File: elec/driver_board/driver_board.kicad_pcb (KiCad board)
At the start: 2 copper layers, 263.5 x 52 mm, 110 parts, among them IC1 TPIC6C595DG4, IC10 TPIC6C595DG4, IC11 TPIC6C595DG4, IC12 TPIC6C595DG4, IC13 TPIC6C595DG4, IC14 TPIC6C595DG4, IC15 TPIC6C595DG4, IC16 TPIC6C595DG4, IC17 TPIC6C595DG4, IC18 TPIC6C595DG4, IC19 TPIC6C595DG4, IC2 TPIC6C595DG4, IC20 TPIC6C595DG4, IC21 TPIC6C595DG4, IC22 TPIC6C595DG4, IC23 TPIC6C595DG4, IC24 TPIC6C595DG4, IC3 TPIC6C595DG4, IC4 TPIC6C595DG4, IC5 TPIC6C595DG4, IC6 TPIC6C595DG4, IC7 TPIC6C595DG4, IC8 TPIC6C595DG4, IC9 TPIC6C595DG4, J1 Connector to the motor board, J10 Connector to the motor board, J11 Connector to the motor board, J12 Connector to the motor board, J13 Connector to the motor board, J14 Connector to the motor board, J15 Connector to the motor board, J16 Connector to the motor board, J17 Connector to the motor board, J18 Connector to the motor board, J19 Connector to the motor board, J2 Connector to the motor board, J20 Connector to the motor board, J21 Connector to the motor board, J22 Connector to the motor board, J23 Connector to the motor board, J24 Connector to the motor board, J25 button_shutdown, J26 button_mode, J27 rotary_encoder, J28 DCF77 board, J29 RTC, J3 Connector to the motor board, J4 Connector to the motor board, J5 Connector to the motor board, J6 Connector to the motor board, J7 Connector to the motor board, J8 Connector to the motor board, J9 Connector to the motor board, U1 ESP32-C3-DEVKITM-1

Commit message: [elec] First version of the routing of driver board
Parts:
- added Cl2: 4.2nF, Capacitor_SMD:C_1206_3216Metric, F.Cu at (81.5, 151.8)
- added Rl2: 4.7k, Capacitor_SMD:C_1206_3216Metric, F.Cu at (81.5, 149.2)
- moved C31 156.5 mm to (88.6, 129.4), turned to 180 degrees
- moved C32 151.1 mm to (88.6, 125.4), turned to 180 degrees
- moved J19 148.4 mm to (117.5, 108.2), turned to 90 degrees
- moved J6 147.6 mm to (161.3, 157.5), turned to 90 degrees
- moved J7 144.6 mm to (175.9, 157.5), turned to 90 degrees
- moved J17 144.2 mm to (88.2, 108.2), turned to 90 degrees
- moved C37 142.8 mm to (124.8, 93.8), turned to 0 degrees
- moved C38 141.3 mm to (124.8, 97.8), turned to 0 degrees
- moved IC16 141.0 mm to (88.3, 118.0), turned to 180 degrees
- moved C33 140.9 mm to (95.5, 93.8), turned to 0 degrees
- moved J18 140.5 mm to (102.9, 108.2), turned to 90 degrees
- moved IC6 139.3 mm to (168.9, 154.4), turned to 0 degrees
- moved J1 139.2 mm to (88.2, 157.5), turned to 90 degrees
- moved C34 138.8 mm to (95.5, 97.8), turned to 0 degrees
- moved IC19 138.5 mm to (125.1, 105.2), turned to 0 degrees
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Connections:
- net HALL_IN renamed HALL_0_OUTPUT
- J1 pad 10: unconnected-(J1-Pin_10-Pad10) -> HALL_1_OUTPUT
- J10 pad 10: unconnected-(J10-Pin_10-Pad10) -> HALL_1_OUTPUT
- J11 pad 10: unconnected-(J11-Pin_10-Pad10) -> HALL_1_OUTPUT
- J12 pad 10: unconnected-(J12-Pin_10-Pad10) -> HALL_1_OUTPUT
- J13 pad 10: unconnected-(J13-Pin_10-Pad10) -> HALL_1_OUTPUT
- J14 pad 10: unconnected-(J14-Pin_10-Pad10) -> HALL_1_OUTPUT
- J15 pad 10: unconnected-(J15-Pin_10-Pad10) -> HALL_1_OUTPUT
- J16 pad 10: unconnected-(J16-Pin_10-Pad10) -> HALL_1_OUTPUT
- J17 pad 10: unconnected-(J17-Pin_10-Pad10) -> HALL_1_OUTPUT
- J18 pad 10: unconnected-(J18-Pin_10-Pad10) -> HALL_1_OUTPUT
- J19 pad 10: unconnected-(J19-Pin_10-Pad10) -> HALL_1_OUTPUT
- J2 pad 10: unconnected-(J2-Pin_10-Pad10) -> HALL_1_OUTPUT
- J20 pad 10: unconnected-(J20-Pin_10-Pad10) -> HALL_1_OUTPUT
- J21 pad 10: unconnected-(J21-Pin_10-Pad10) -> HALL_1_OUTPUT
- J22 pad 10: unconnected-(J22-Pin_10-Pad10) -> HALL_1_OUTPUT
- J23 pad 10: unconnected-(J23-Pin_10-Pad10) -> HALL_1_OUTPUT
- J24 pad 10: unconnected-(J24-Pin_10-Pad10) -> HALL_1_OUTPUT
- J29 pad 3: /control_board/SDA_TRC -> /control_board/SDA_RTC
- J3 pad 10: unconnected-(J3-Pin_10-Pad10) -> HALL_1_OUTPUT
- J4 pad 10: unconnected-(J4-Pin_10-Pad10) -> HALL_1_OUTPUT
- J5 pad 10: unconnected-(J5-Pin_10-Pad10) -> HALL_1_OUTPUT
- J6 pad 10: unconnected-(J6-Pin_10-Pad10) -> HALL_1_OUTPUT
- J7 pad 10: unconnected-(J7-Pin_10-Pad10) -> HALL_1_OUTPUT
- J8 pad 10: unconnected-(J8-Pin_10-Pad10) -> HALL_1_OUTPUT
- J9 pad 10: unconnected-(J9-Pin_10-Pad10) -> HALL_1_OUTPUT
- U1 pad 21: unconnected-(U1-IO5-Pad21) -> HALL_1_OUTPUT
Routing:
- net HALL_1_OUTPUT: track 0.00 -> 399.0 mm, vias 0 -> 1
- net VCC_3V3: track 0.00 -> 126.5 mm
- net SHIFT_CLOCK: track 572.2 -> 482.1 mm, vias 24 -> 26
- net /control_board/AM_DATA: track 0.00 -> 64.9 mm, vias 0 -> 1
- net VCC: track 720.5 -> 781.4 mm, vias 46 -> 50
- net LATCH_CLOCK: track 500.2 -> 442.1 mm
- net /control_board/PIN_BUTTON_ENCODER: track 0.00 -> 47.6 mm, vias 0 -> 1
- net /control_board/DATA_OUT: track 59.4 -> 18.8 mm
- net /control_board/PIN_ENCODER_1: track 0.00 -> 40.4 mm, vias 0 -> 1
- net /control_board/PIN_ENCODER_0: track 0.00 -> 37.7 mm, vias 0 -> 1
- net /motor_driver10/DATA_IN: track 58.9 -> 22.0 mm, vias 4 -> 0
- net /control_board/SDA_RTC: track 0.00 -> 36.7 mm
- net /control_board/SCL_RTC: track 0.00 -> 34.6 mm
- net /motor_driver8/DATA_OUT: track 55.4 -> 22.2 mm
- net /motor_driver5/DATA_OUT: track 54.8 -> 22.0 mm
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- added copper zone on B.Cu, net GND
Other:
- board size 263.5 x 52 mm -> 170.8 x 83 mm
- board text added: "Driver board V1 26/11/2024"

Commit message: [elec] Add space for physical button
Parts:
- added S1: FSM2JAH, Samacsys:FSM4JH, F.Cu at (42.5, 145.5)
- added S2: FSM2JAH, Samacsys:FSM4JH, F.Cu at (49.0, 145.5)
- Cl1, Cl2: value 4.2nF -> 4.7nF
- moved J25 6.49 mm to (43.5, 156.5)
- moved J26 6.49 mm to (48.0, 156.5)
- moved R1 6.49 mm to (43.5, 152.5)
- moved R2 6.49 mm to (51.0, 155.5)
- moved JP1 5.02 mm to (47.0, 162.8)
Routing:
- net VCC_3V3: track 126.5 -> 151.4 mm
- net /control_board/PIN_BUTTON_MODE: track 6.46 -> 15.9 mm
- net VCC: track 781.4 -> 786.2 mm
- net /control_board/PIN_BUTTON_SHUTDOWN: track 15.0 -> 18.0 mm
- added copper zone on F.Cu, net VCC
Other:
- board size 170.8 x 83 mm -> 171.8 x 83 mm
- board text added: "Driver board v1 26/11/2024"
- board text added: "VCC_3V3"
- board text removed: "Driver board V1 26/11/2024"

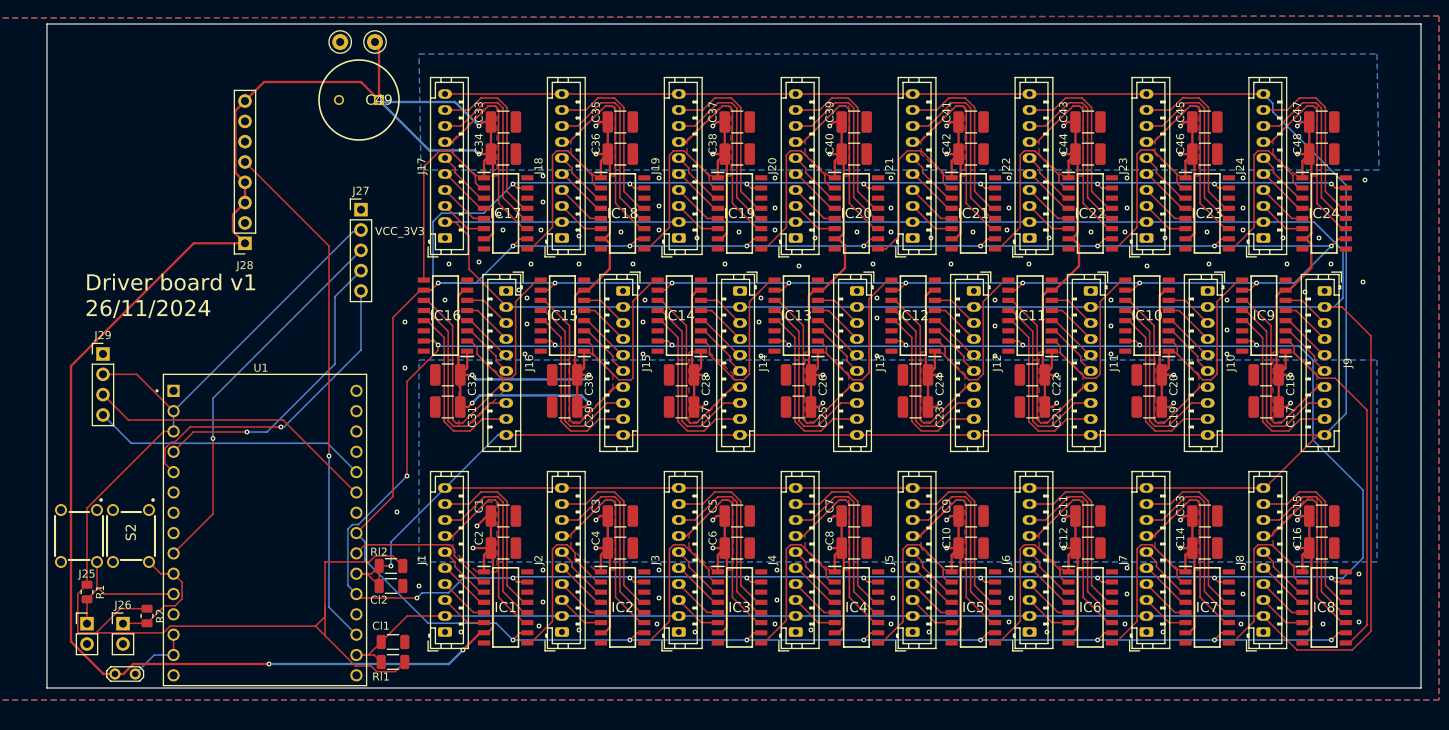
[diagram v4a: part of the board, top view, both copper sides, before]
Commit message: Update BKA30D-R5 dimensions
Also add some silkscreen on both PCB
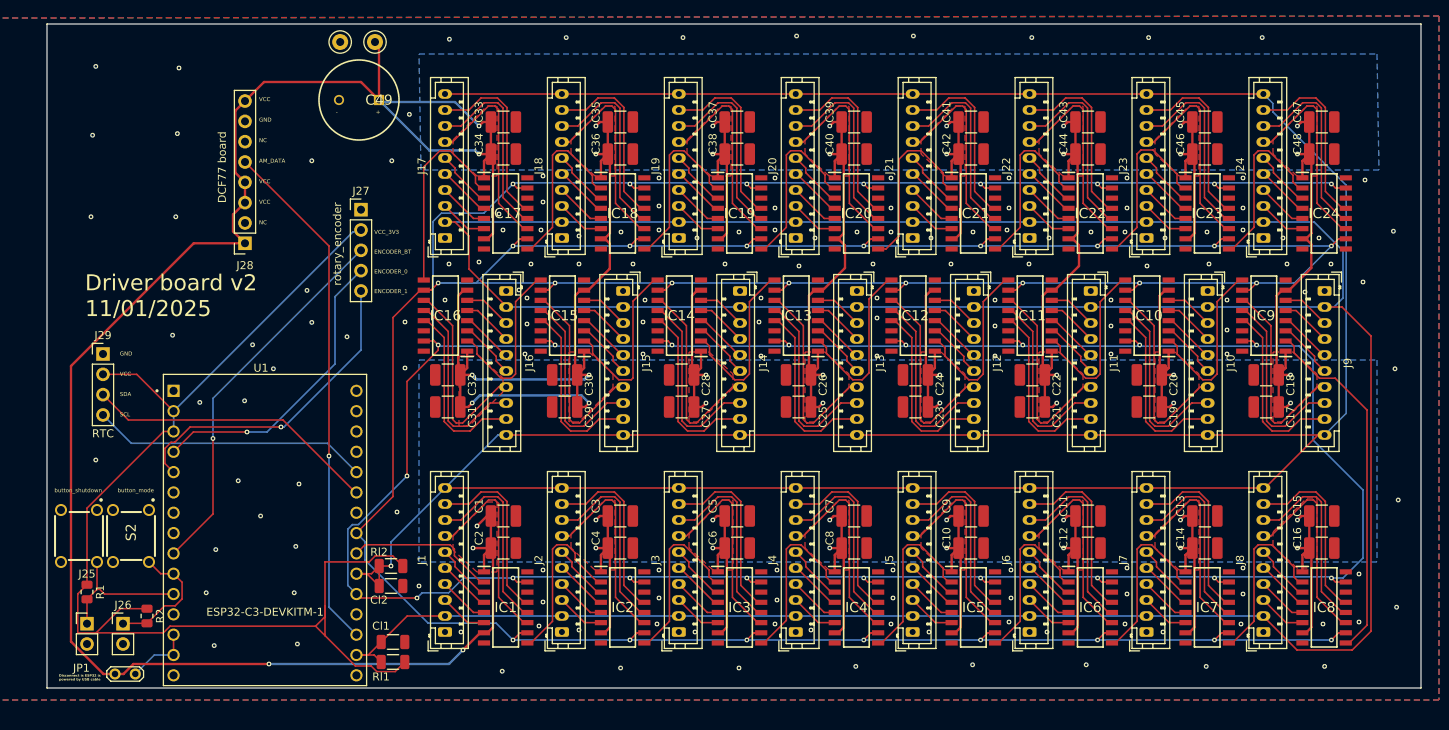
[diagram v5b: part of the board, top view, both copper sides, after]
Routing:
- net GND: vias 112 -> 159
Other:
- board text added: "+"
- board text added: "-"
- board text added: "AM_DATA"
- board text added: "Disconnect is ESP32 is powered by USB cable"
- board text added: "Driver board v2 11/01/2025"
- board text added: "ENCODER_0"
- board text added: "ENCODER_1"
- board text added: "ENCODER_BT"
- board text added: "GND"
- board text added: "NC"
- board text added: "SCL"
- board text added: "SDA"
- board text added: "VCC"
- board text removed: "Driver board v1 26/11/2024"

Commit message: Update schematic with VID6606
Use the 'official' driver of VID28-05 motors.
Put back the 74HCT595 bit shift register to link all
motor drivers.
Work in progress.
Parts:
- removed Cl1, Cl2: 4.7nF, Capacitor_SMD:C_1206_3216Metric
- removed IC1, IC10, IC11, IC12, IC13, IC14, IC15, IC16, IC17, IC18, IC19, IC2, IC20, IC21, IC22, IC23, IC24, IC3, IC4, IC5, IC6, IC7, IC8, IC9: TPIC6C595DG4, Samacsys:SOIC127P600X175-16N
- removed J28: DCF77 board, Connector_PinSocket_2.54mm:PinSocket_1x08_P2.54mm_Vertical
- removed J29: RTC, Connector_PinHeader_2.54mm:PinHeader_1x04_P2.54mm_Vertical
- removed Rl1, Rl2: 4.7k, Capacitor_SMD:C_1206_3216Metric
- added C50: 100nF, Capacitor_SMD:C_0805_2012Metric, F.Cu at (96.8, 30.6)
- added C51: 4.7µF, Capacitor_SMD:C_0805_2012Metric, B.Cu at (101.4, 48.6)
- added C52: 100nF, Capacitor_SMD:C_0805_2012Metric, F.Cu at (75.0, 53.8)
- added C53: 4.7µF, Capacitor_SMD:C_0805_2012Metric, F.Cu at (71.7, 53.8)
- added C54: 100nF, Capacitor_SMD:C_0805_2012Metric, F.Cu at (63.0, 30.6)
- added C55: 100nF, Capacitor_SMD:C_0805_2012Metric, F.Cu at (66.4, 30.6)
- added C56: 4.7µF, Capacitor_SMD:C_0805_2012Metric, B.Cu at (71.0, 48.6)
- added C57: 100nF, Capacitor_SMD:C_0805_2012Metric, F.Cu at (105.4, 88.6)
- added C58: 4.7µF, Capacitor_SMD:C_0805_2012Metric, F.Cu at (102.1, 88.6)
- added C59: 100nF, Capacitor_SMD:C_0805_2012Metric, F.Cu at (93.4, 65.4)
- added C60: 100nF, Capacitor_SMD:C_0805_2012Metric, F.Cu at (96.8, 65.4)
- added C61: 4.7µF, Capacitor_SMD:C_0805_2012Metric, B.Cu at (101.4, 83.4)
- added U10: 74HCT595, Package_SO:SOIC-16_3.9x9.9mm_P1.27mm, B.Cu at (129.8, 42.2)
- added U11: ~, Package_SO:SOP-28_8.4x18.16mm_P1.27mm, F.Cu at (129.8, 42.3)
- added U12: 74HCT595, Package_SO:SOIC-16_3.9x9.9mm_P1.27mm, B.Cu at (129.8, 111.8)
- added U13: ~, Package_SO:SOP-28_8.4x18.16mm_P1.27mm, F.Cu at (129.8, 111.9)
- added U14: 74HCT595, Package_SO:SOIC-16_3.9x9.9mm_P1.27mm, B.Cu at (69.0, 146.7)
- added U15: ~, Package_SO:SOP-28_8.4x18.16mm_P1.27mm, F.Cu at (69.0, 146.7)
- added U16: 74HCT595, Package_SO:SOIC-16_3.9x9.9mm_P1.27mm, B.Cu at (129.8, 77.0)
- added U17: ~, Package_SO:SOP-28_8.4x18.16mm_P1.27mm, F.Cu at (129.8, 77.1)
- added U18: 74HCT595, Package_SO:SOIC-16_3.9x9.9mm_P1.27mm, B.Cu at (24.4, 90.0)
- added U19: ~, Package_SO:SOP-28_8.4x18.16mm_P1.27mm, F.Cu at (24.4, 90.1)
- added U2: 74HCT595, Package_SO:SOIC-16_3.9x9.9mm_P1.27mm, B.Cu at (190.2, 110.5)
- added U20: 74HCT595, Package_SO:SOIC-16_3.9x9.9mm_P1.27mm, B.Cu at (99.4, 42.2)
- added U21: ~, Package_SO:SOP-28_8.4x18.16mm_P1.27mm, F.Cu at (99.4, 42.3)
- added U22: 74HCT595, Package_SO:SOIC-16_3.9x9.9mm_P1.27mm, B.Cu at (69.0, 42.2)
- added U23: ~, Package_SO:SOP-28_8.4x18.16mm_P1.27mm, F.Cu at (69.0, 42.3)
- added U24: 74HCT595, Package_SO:SOIC-16_3.9x9.9mm_P1.27mm, B.Cu at (99.4, 77.0)
- added U25: ~, Package_SO:SOP-28_8.4x18.16mm_P1.27mm, F.Cu at (99.4, 77.1)
- added U3: ~, Package_SO:SOP-28_8.4x18.16mm_P1.27mm, F.Cu at (190.2, 110.6)
- added U4: 74HCT595, Package_SO:SOIC-16_3.9x9.9mm_P1.27mm, B.Cu at (225.8, 110.3)
- added U5: ~, Package_SO:SOP-28_8.4x18.16mm_P1.27mm, F.Cu at (225.8, 110.4)
- added U6: 74HCT595, Package_SO:SOIC-16_3.9x9.9mm_P1.27mm, B.Cu at (69.0, 77.0)
- added U7: ~, Package_SO:SOP-28_8.4x18.16mm_P1.27mm, F.Cu at (69.0, 77.1)
- added U8: 74HCT595, Package_SO:SOIC-16_3.9x9.9mm_P1.27mm, B.Cu at (24.4, 124.8)
- added U9: ~, Package_SO:SOP-28_8.4x18.16mm_P1.27mm, F.Cu at (24.4, 124.9)
- C1: value 47µF -> ECA-1HM471; footprint Capacitor_SMD:C_1210_3225Metric_Pad1.33x2.70mm_HandSolder -> Samacsys:CAPPRD500W65D1000H2200
- C10, C12, C14, C2, C20, C22, C24, C30, C32, C34, C4, C40, C42, C44: value 0.1µF -> 100nF; footprint Capacitor_SMD:C_1210_3225Metric_Pad1.33x2.70mm_HandSolder -> Capacitor_SMD:C_0805_2012Metric
- C11, C21, C31, C41: value 47µF -> 4.7µF; footprint Capacitor_SMD:C_1210_3225Metric_Pad1.33x2.70mm_HandSolder -> Capacitor_SMD:C_0805_2012Metric; moved to B.Cu
- C13, C23, C3, C33, C43: value 47µF -> 4.7µF; footprint Capacitor_SMD:C_1210_3225Metric_Pad1.33x2.70mm_HandSolder -> Capacitor_SMD:C_0805_2012Metric
- C15, C17, C19, C25, C27, C29, C35, C37, C39, C45, C47, C5, C7, C9: value 47µF -> 100nF; footprint Capacitor_SMD:C_1210_3225Metric_Pad1.33x2.70mm_HandSolder -> Capacitor_SMD:C_0805_2012Metric
- C16, C26, C36, C46, C6: value 0.1µF -> 4.7µF; footprint Capacitor_SMD:C_1210_3225Metric_Pad1.33x2.70mm_HandSolder -> Capacitor_SMD:C_0805_2012Metric; moved to B.Cu
- C18, C28, C38, C48, C8: value 0.1µF -> 4.7µF; footprint Capacitor_SMD:C_1210_3225Metric_Pad1.33x2.70mm_HandSolder -> Capacitor_SMD:C_0805_2012Metric
- C49: value ECA-1HM471 -> 100nF; footprint Samacsys:CAPPRD500W65D1000H2200 -> Capacitor_SMD:C_0805_2012Metric
- J1: value Connector to the motor board -> rotary_encoder; footprint Connector_JST:JST_PH_B10B-PH-K_1x10_P2.00mm_Vertical -> Connector_PinHeader_2.54mm:PinHeader_1x05_P2.54mm_Vertical
- J10, J12, J14, J16, J18, J20, J22, J24, J4, J6, J8: value Connector to the motor board -> Conn motor 0; footprint Connector_JST:JST_PH_B10B-PH-K_1x10_P2.00mm_Vertical -> Connector_JST:JST_PH_B8B-PH-K_1x08_P2.00mm_Vertical
- J11, J13, J15, J17, J19, J21, J23, J5, J7, J9: value Connector to the motor board -> Conn motor 1; footprint Connector_JST:JST_PH_B10B-PH-K_1x10_P2.00mm_Vertical -> Connector_JST:JST_PH_B8B-PH-K_1x08_P2.00mm_Vertical
- J2: value Connector to the motor board -> DCF77 board; footprint Connector_JST:JST_PH_B10B-PH-K_1x10_P2.00mm_Vertical -> Connector_PinSocket_2.54mm:PinSocket_1x08_P2.54mm_Vertical
- J25: value button_shutdown -> Conn motor 1; footprint Connector_PinHeader_2.54mm:PinHeader_1x02_P2.54mm_Vertical -> Connector_JST:JST_PH_B8B-PH-K_1x08_P2.00mm_Vertical
- J26: value button_mode -> Conn motor 0; footprint Connector_PinHeader_2.54mm:PinHeader_1x02_P2.54mm_Vertical -> Connector_JST:JST_PH_B8B-PH-K_1x08_P2.00mm_Vertical
- J27: value rotary_encoder -> Conn motor 1; footprint Connector_PinHeader_2.54mm:PinHeader_1x05_P2.54mm_Vertical -> Connector_JST:JST_PH_B8B-PH-K_1x08_P2.00mm_Vertical
- J3: value Connector to the motor board -> RTC; footprint Connector_JST:JST_PH_B10B-PH-K_1x10_P2.00mm_Vertical -> Connector_PinHeader_2.54mm:PinHeader_1x04_P2.54mm_Vertical
- S1: value FSM2JAH -> Button shutdown
- S2: value FSM2JAH -> Button mode
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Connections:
- J1 pad 2: HALL_0_OUTPUT -> /control_board/VCC_3V3
- J1 pad 3: /motor_driver0/M1_1 -> /control_board/PIN_BUTTON_ENCODER
- J1 pad 4: /motor_driver0/M0_4 -> /control_board/PIN_ENCODER_0
- J1 pad 5: /motor_driver0/M0_23 -> /control_board/PIN_ENCODER_1
- J10 pad 1: GND -> /motor_driver3/A3
- J10 pad 2: HALL_0_OUTPUT -> /motor_driver3/A4
- J10 pad 3: /motor_driver9/M1_1 -> /motor_driver3/A2
- J10 pad 4: /motor_driver9/M0_4 -> /motor_driver3/A1
- J10 pad 5: /motor_driver9/M0_23 -> /motor_driver3/D1
- J10 pad 6: /motor_driver9/M0_1 -> /motor_driver3/D2
- J10 pad 7: /motor_driver9/M1_23 -> /motor_driver3/D4
- J10 pad 8: /motor_driver9/M1_4 -> /motor_driver3/D3
- J11 pad 1: GND -> /motor_driver3/C3
- J11 pad 2: HALL_0_OUTPUT -> /motor_driver3/C4
- J11 pad 3: /motor_driver10/M1_1 -> /motor_driver3/C2
- J11 pad 4: /motor_driver10/M0_4 -> /motor_driver3/C1
- J11 pad 5: /motor_driver10/M0_23 -> /motor_driver3/B1
- J11 pad 6: /motor_driver10/M0_1 -> /motor_driver3/B2
- J11 pad 7: /motor_driver10/M1_23 -> /motor_driver3/B4
- J11 pad 8: /motor_driver10/M1_4 -> /motor_driver3/B3
- J12 pad 1: GND -> /motor_driver4/A3
- J12 pad 2: HALL_0_OUTPUT -> /motor_driver4/A4
- J12 pad 3: /motor_driver11/M1_1 -> /motor_driver4/A2
- J12 pad 4: /motor_driver11/M0_4 -> /motor_driver4/A1
- J12 pad 5: /motor_driver11/M0_23 -> /motor_driver4/D1
- J12 pad 6: /motor_driver11/M0_1 -> /motor_driver4/D2
- J12 pad 7: /motor_driver11/M1_23 -> /motor_driver4/D4
- J12 pad 8: /motor_driver11/M1_4 -> /motor_driver4/D3
- J13 pad 1: GND -> /motor_driver4/C3
- J13 pad 2: HALL_0_OUTPUT -> /motor_driver4/C4
- J13 pad 3: /motor_driver12/M1_1 -> /motor_driver4/C2
- J13 pad 4: /motor_driver12/M0_4 -> /motor_driver4/C1
- J13 pad 5: /motor_driver12/M0_23 -> /motor_driver4/B1
- J13 pad 6: /motor_driver12/M0_1 -> /motor_driver4/B2
- J13 pad 7: /motor_driver12/M1_23 -> /motor_driver4/B4
- J13 pad 8: /motor_driver12/M1_4 -> /motor_driver4/B3
- J14 pad 1: GND -> /motor_driver5/A3
- J14 pad 2: HALL_0_OUTPUT -> /motor_driver5/A4
- J14 pad 3: /motor_driver13/M1_1 -> /motor_driver5/A2
- J14 pad 4: /motor_driver13/M0_4 -> /motor_driver5/A1
- J14 pad 5: /motor_driver13/M0_23 -> /motor_driver5/D1
- J14 pad 6: /motor_driver13/M0_1 -> /motor_driver5/D2
- J14 pad 7: /motor_driver13/M1_23 -> /motor_driver5/D4
- J14 pad 8: /motor_driver13/M1_4 -> /motor_driver5/D3
- J15 pad 1: GND -> /motor_driver5/C3
- J15 pad 2: HALL_0_OUTPUT -> /motor_driver5/C4
- J15 pad 3: /motor_driver14/M1_1 -> /motor_driver5/C2
- J15 pad 4: /motor_driver14/M0_4 -> /motor_driver5/C1
- J15 pad 5: /motor_driver14/M0_23 -> /motor_driver5/B1
- J15 pad 6: /motor_driver14/M0_1 -> /motor_driver5/B2
- J15 pad 7: /motor_driver14/M1_23 -> /motor_driver5/B4
- J15 pad 8: /motor_driver14/M1_4 -> /motor_driver5/B3
- J16 pad 1: GND -> /motor_driver6/A3
- J16 pad 2: HALL_0_OUTPUT -> /motor_driver6/A4
- J16 pad 3: /motor_driver15/M1_1 -> /motor_driver6/A2
- J16 pad 4: /motor_driver15/M0_4 -> /motor_driver6/A1
- J16 pad 5: /motor_driver15/M0_23 -> /motor_driver6/D1
- J16 pad 6: /motor_driver15/M0_1 -> /motor_driver6/D2
- J16 pad 7: /motor_driver15/M1_23 -> /motor_driver6/D4
- J16 pad 8: /motor_driver15/M1_4 -> /motor_driver6/D3
- J17 pad 1: GND -> /motor_driver6/C3
- J17 pad 2: HALL_0_OUTPUT -> /motor_driver6/C4
- J17 pad 3: /motor_driver16/M1_1 -> /motor_driver6/C2
- J17 pad 4: /motor_driver16/M0_4 -> /motor_driver6/C1
- J17 pad 5: /motor_driver16/M0_23 -> /motor_driver6/B1
- J17 pad 6: /motor_driver16/M0_1 -> /motor_driver6/B2
- J17 pad 7: /motor_driver16/M1_23 -> /motor_driver6/B4
- J17 pad 8: /motor_driver16/M1_4 -> /motor_driver6/B3
- J18 pad 1: GND -> /motor_driver7/A3
- J18 pad 2: HALL_0_OUTPUT -> /motor_driver7/A4
- J18 pad 3: /motor_driver17/M1_1 -> /motor_driver7/A2
- J18 pad 4: /motor_driver17/M0_4 -> /motor_driver7/A1
- J18 pad 5: /motor_driver17/M0_23 -> /motor_driver7/D1
- J18 pad 6: /motor_driver17/M0_1 -> /motor_driver7/D2
- J18 pad 7: /motor_driver17/M1_23 -> /motor_driver7/D4
- J18 pad 8: /motor_driver17/M1_4 -> /motor_driver7/D3
- J19 pad 1: GND -> /motor_driver7/C3
- J19 pad 2: HALL_0_OUTPUT -> /motor_driver7/C4
- J19 pad 3: /motor_driver18/M1_1 -> /motor_driver7/C2
- J19 pad 4: /motor_driver18/M0_4 -> /motor_driver7/C1
- J19 pad 5: /motor_driver18/M0_23 -> /motor_driver7/B1
- J19 pad 6: /motor_driver18/M0_1 -> /motor_driver7/B2
- J19 pad 7: /motor_driver18/M1_23 -> /motor_driver7/B4
- J19 pad 8: /motor_driver18/M1_4 -> /motor_driver7/B3
- J2 pad 1: GND -> VCC
- J2 pad 2: HALL_0_OUTPUT -> unconnected-(J2-Pin_2-Pad2)
- J2 pad 3: /motor_driver1/M1_1 -> VCC
- J2 pad 4: /motor_driver1/M0_4 -> VCC
- J2 pad 5: /motor_driver1/M0_23 -> /control_board/AM_DATA
- J2 pad 6: /motor_driver1/M0_1 -> unconnected-(J2-Pin_6-Pad6)
- J2 pad 7: /motor_driver1/M1_23 -> GND
- J2 pad 8: /motor_driver1/M1_4 -> VCC
- J20 pad 1: GND -> /motor_driver8/A3
- J20 pad 2: HALL_0_OUTPUT -> /motor_driver8/A4
- J20 pad 3: /motor_driver19/M1_1 -> /motor_driver8/A2
- J20 pad 4: /motor_driver19/M0_4 -> /motor_driver8/A1
- J20 pad 5: /motor_driver19/M0_23 -> /motor_driver8/D1
- J20 pad 6: /motor_driver19/M0_1 -> /motor_driver8/D2
- J20 pad 7: /motor_driver19/M1_23 -> /motor_driver8/D4
- J20 pad 8: /motor_driver19/M1_4 -> /motor_driver8/D3
- J21 pad 1: GND -> /motor_driver8/C3
- J21 pad 2: HALL_0_OUTPUT -> /motor_driver8/C4
- J21 pad 3: /motor_driver20/M1_1 -> /motor_driver8/C2
- J21 pad 4: /motor_driver20/M0_4 -> /motor_driver8/C1
- J21 pad 5: /motor_driver20/M0_23 -> /motor_driver8/B1
- J21 pad 6: /motor_driver20/M0_1 -> /motor_driver8/B2
- J21 pad 7: /motor_driver20/M1_23 -> /motor_driver8/B4
- J21 pad 8: /motor_driver20/M1_4 -> /motor_driver8/B3
- J22 pad 1: GND -> /motor_driver9/A3
- J22 pad 2: HALL_0_OUTPUT -> /motor_driver9/A4
- J22 pad 3: /motor_driver21/M1_1 -> /motor_driver9/A2
- J22 pad 4: /motor_driver21/M0_4 -> /motor_driver9/A1
- J22 pad 5: /motor_driver21/M0_23 -> /motor_driver9/D1
- J22 pad 6: /motor_driver21/M0_1 -> /motor_driver9/D2
- J22 pad 7: /motor_driver21/M1_23 -> /motor_driver9/D4
- J22 pad 8: /motor_driver21/M1_4 -> /motor_driver9/D3
- J23 pad 1: GND -> /motor_driver9/C3
- J23 pad 2: HALL_0_OUTPUT -> /motor_driver9/C4
- J23 pad 3: /motor_driver22/M1_1 -> /motor_driver9/C2
- J23 pad 4: /motor_driver22/M0_4 -> /motor_driver9/C1
- J23 pad 5: /motor_driver22/M0_23 -> /motor_driver9/B1
- J23 pad 6: /motor_driver22/M0_1 -> /motor_driver9/B2
- J23 pad 7: /motor_driver22/M1_23 -> /motor_driver9/B4
- J23 pad 8: /motor_driver22/M1_4 -> /motor_driver9/B3
- J24 pad 1: GND -> /motor_driver10/A3
- J24 pad 2: HALL_0_OUTPUT -> /motor_driver10/A4
- J24 pad 3: /motor_driver23/M1_1 -> /motor_driver10/A2
- J24 pad 4: /motor_driver23/M0_4 -> /motor_driver10/A1
- J24 pad 5: /motor_driver23/M0_23 -> /motor_driver10/D1
- J24 pad 6: /motor_driver23/M0_1 -> /motor_driver10/D2
- J24 pad 7: /motor_driver23/M1_23 -> /motor_driver10/D4
- J24 pad 8: /motor_driver23/M1_4 -> /motor_driver10/D3
- J25 pad 1: /control_board/PIN_BUTTON_SHUTDOWN -> /motor_driver10/C3
- J25 pad 2: GND -> /motor_driver10/C4
- J26 pad 1: /control_board/PIN_BUTTON_MODE -> /motor_driver11/A3
- J26 pad 2: GND -> /motor_driver11/A4
- J27 pad 1: GND -> /motor_driver11/C3
- J27 pad 2: VCC_3V3 -> /motor_driver11/C4
- J27 pad 3: /control_board/PIN_BUTTON_ENCODER -> /motor_driver11/C2
- J27 pad 4: /control_board/PIN_ENCODER_0 -> /motor_driver11/C1
- J27 pad 5: /control_board/PIN_ENCODER_1 -> /motor_driver11/B1
- J3 pad 2: HALL_0_OUTPUT -> /control_board/VCC_3V3
- J3 pad 3: /motor_driver2/M1_1 -> /control_board/SDA_RTC
- J3 pad 4: /motor_driver2/M0_4 -> /control_board/SCL_RTC
- J4 pad 1: GND -> /motor_driver0/A3
- J4 pad 2: HALL_0_OUTPUT -> /motor_driver0/A4
- J4 pad 3: /motor_driver3/M1_1 -> /motor_driver0/A2
- J4 pad 4: /motor_driver3/M0_4 -> /motor_driver0/A1
- J4 pad 5: /motor_driver3/M0_23 -> /motor_driver0/D1
- J4 pad 6: /motor_driver3/M0_1 -> /motor_driver0/D2
- J4 pad 7: /motor_driver3/M1_23 -> /motor_driver0/D4
- J4 pad 8: /motor_driver3/M1_4 -> /motor_driver0/D3
- J5 pad 1: GND -> /motor_driver0/C3
- J5 pad 2: HALL_0_OUTPUT -> /motor_driver0/C4
- J5 pad 3: /motor_driver4/M1_1 -> /motor_driver0/C2
- J5 pad 4: /motor_driver4/M0_4 -> /motor_driver0/C1
- J5 pad 5: /motor_driver4/M0_23 -> /motor_driver0/B1
- J5 pad 6: /motor_driver4/M0_1 -> /motor_driver0/B2
- J5 pad 7: /motor_driver4/M1_23 -> /motor_driver0/B4
- J5 pad 8: /motor_driver4/M1_4 -> /motor_driver0/B3
- J6 pad 1: GND -> /motor_driver1/A3
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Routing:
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- removed copper zone on B.Cu, net VCC
- removed copper zone on F.Cu, net VCC
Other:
- board outline removed
- board text removed: "+"
- board text removed: "-"
- board text removed: "AM_DATA"
- board text removed: "Disconnect is ESP32 is powered by USB cable"
- board text removed: "Driver board v2 11/01/2025"
- board text removed: "ENCODER_0"
- board text removed: "ENCODER_1"
- board text removed: "ENCODER_BT"
- board text removed: "GND"
- board text removed: "NC"
- board text removed: "SCL"
- board text removed: "SDA"
- board text removed: "VCC"
- board text removed: "VCC_3V3"

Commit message: New schematic + route
The new design schematic is done.
Route is ongoing
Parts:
- added C62: 100nF, Capacitor_SMD:C_0805_2012Metric, F.Cu at (107.4, 126.9)
- added C63: 4.7µF, Capacitor_SMD:C_0805_2012Metric, F.Cu at (97.4, 98.9)
- added U26: ~, Package_SO:SOP-28_8.4x18.16mm_P1.27mm, F.Cu at (103.5, 115.8)
- C1: value ECA-1HM471 -> 100nF; footprint Samacsys:CAPPRD500W65D1000H2200 -> Capacitor_SMD:C_0805_2012Metric
- C10, C15, C20, C25, C30, C35, C40, C45, C5, C50, C55, C60: value 100nF -> 4.7µF
- C11, C16, C21, C26, C31, C36, C41, C46, C51, C56, C6, C61: value 4.7µF -> 100nF; moved to F.Cu
- C3: value 4.7µF -> ECA-1HM471; footprint Capacitor_SMD:C_0805_2012Metric -> Samacsys:CAPPRD500W65D1000H2200
- U10, U12, U14, U16, U18, U20, U22, U24, U4, U6, U8: value 74HCT595 -> ~; footprint Package_SO:SOIC-16_3.9x9.9mm_P1.27mm -> Package_SO:SOP-28_8.4x18.16mm_P1.27mm; moved to F.Cu
- U11, U13, U15, U17, U19, U21, U23, U25, U3, U5, U7, U9: value ~ -> 74HCT595; footprint Package_SO:SOP-28_8.4x18.16mm_P1.27mm -> Package_SO:SOIC-16_3.9x9.9mm_P1.27mm
- U2: value 74HCT595 -> TXB0102DCT; footprint Package_SO:SOIC-16_3.9x9.9mm_P1.27mm -> Package_SO:TSSOP-8_3x3mm_P0.65mm; moved to F.Cu
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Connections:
- C1 pad 1: VCC -> /control_board/VCC_3V3
- J2 pad 1: VCC -> GND
- J2 pad 2: unconnected-(J2-Pin_2-Pad2) -> GND
- J2 pad 3: VCC -> unconnected-(J2-Pin_3-Pad3)
- J2 pad 4: VCC -> /control_board/AM_DATA
- J2 pad 5: /control_board/AM_DATA -> unconnected-(J2-Pin_5-Pad5)
- J2 pad 7: GND -> VCC
- J2 pad 8: VCC -> unconnected-(J2-Pin_8-Pad8)
- U1 pad 17: Reset -> unconnected-(U1-IO19-Pad17)
- U1 pad 20: SHIFT_CLOCK -> /control_board/SHIFT_CLOCK_3V3
- U1 pad 23: LATCH_CLOCK -> /control_board/LATCH_CLOCK_3V3
- U10 pad 1: /motor_driver4/DIR_D -> VCC
- U10 pad 10: Reset -> /motor_driver3/D4
- U10 pad 11: SHIFT_CLOCK -> /motor_driver3/D3
- U10 pad 12: LATCH_CLOCK -> GND
- U10 pad 13: GND -> /motor_driver3/DIR_C
- U10 pad 14: /motor_driver3/DATA_OUT -> /motor_driver3/STEP_C
- U10 pad 15: /motor_driver4/DIR_A -> VCC
- U10 pad 16: VCC -> /motor_driver3/DIR_D
- U10 pad 2: /motor_driver4/STEP_D -> /motor_driver3/DIR_B
- U10 pad 3: /motor_driver4/STEP_A -> /motor_driver3/STEP_B
- U10 pad 4: /motor_driver4/STEP_C -> /motor_driver3/A3
- U10 pad 5: /motor_driver4/DIR_C -> /motor_driver3/A4
- U10 pad 6: /motor_driver4/STEP_B -> /motor_driver3/A2
- U10 pad 7: /motor_driver4/DIR_B -> /motor_driver3/A1
- U10 pad 8: GND -> /motor_driver3/D1
- U10 pad 9: /motor_driver4/DATA_OUT -> /motor_driver3/D2
- U11 pad 1: VCC -> /motor_driver4/STEP_D
- U11 pad 10: /motor_driver4/D4 -> VCC
- U11 pad 11: /motor_driver4/D3 -> SHIFT_CLOCK
- U11 pad 12: GND -> LATCH_CLOCK
- U11 pad 13: /motor_driver4/DIR_C -> GND
- U11 pad 14: /motor_driver4/STEP_C -> /motor_driver3/DATA_OUT
- U11 pad 15: VCC -> /motor_driver4/DIR_D
- U11 pad 16: /motor_driver4/DIR_D -> VCC
- U11 pad 2: /motor_driver4/DIR_B -> /motor_driver4/DIR_A
- U11 pad 3: /motor_driver4/STEP_B -> /motor_driver4/STEP_A
- U11 pad 4: /motor_driver4/A3 -> /motor_driver4/DIR_B
- U11 pad 5: /motor_driver4/A4 -> /motor_driver4/STEP_B
- U11 pad 6: /motor_driver4/A2 -> /motor_driver4/DIR_C
- U11 pad 7: /motor_driver4/A1 -> /motor_driver4/STEP_C
- U11 pad 8: /motor_driver4/D1 -> GND
- U11 pad 9: /motor_driver4/D2 -> /motor_driver4/DATA_OUT
- U12 pad 1: /motor_driver5/DIR_D -> VCC
- U12 pad 10: Reset -> /motor_driver4/D4
- U12 pad 11: SHIFT_CLOCK -> /motor_driver4/D3
- U12 pad 12: LATCH_CLOCK -> GND
- U12 pad 13: GND -> /motor_driver4/DIR_C
- U12 pad 14: /motor_driver4/DATA_OUT -> /motor_driver4/STEP_C
- U12 pad 15: /motor_driver5/DIR_A -> VCC
- U12 pad 16: VCC -> /motor_driver4/DIR_D
- U12 pad 2: /motor_driver5/STEP_D -> /motor_driver4/DIR_B
- U12 pad 3: /motor_driver5/STEP_A -> /motor_driver4/STEP_B
- U12 pad 4: /motor_driver5/STEP_C -> /motor_driver4/A3
- U12 pad 5: /motor_driver5/DIR_C -> /motor_driver4/A4
- U12 pad 6: /motor_driver5/STEP_B -> /motor_driver4/A2
- U12 pad 7: /motor_driver5/DIR_B -> /motor_driver4/A1
- U12 pad 8: GND -> /motor_driver4/D1
- U12 pad 9: /motor_driver5/DATA_OUT -> /motor_driver4/D2
- U13 pad 1: VCC -> /motor_driver5/STEP_D
- U13 pad 10: /motor_driver5/D4 -> VCC
- U13 pad 11: /motor_driver5/D3 -> SHIFT_CLOCK
- U13 pad 12: GND -> LATCH_CLOCK
- U13 pad 13: /motor_driver5/DIR_C -> GND
- U13 pad 14: /motor_driver5/STEP_C -> /motor_driver4/DATA_OUT
- U13 pad 15: VCC -> /motor_driver5/DIR_D
- U13 pad 16: /motor_driver5/DIR_D -> VCC
- U13 pad 2: /motor_driver5/DIR_B -> /motor_driver5/DIR_A
- U13 pad 3: /motor_driver5/STEP_B -> /motor_driver5/STEP_A
- U13 pad 4: /motor_driver5/A3 -> /motor_driver5/DIR_B
- U13 pad 5: /motor_driver5/A4 -> /motor_driver5/STEP_B
- U13 pad 6: /motor_driver5/A2 -> /motor_driver5/DIR_C
- U13 pad 7: /motor_driver5/A1 -> /motor_driver5/STEP_C
- U13 pad 8: /motor_driver5/D1 -> GND
- U13 pad 9: /motor_driver5/D2 -> /motor_driver5/DATA_OUT
- U14 pad 1: /motor_driver6/DIR_D -> VCC
- U14 pad 10: Reset -> /motor_driver5/D4
- U14 pad 11: SHIFT_CLOCK -> /motor_driver5/D3
- U14 pad 12: LATCH_CLOCK -> GND
- U14 pad 13: GND -> /motor_driver5/DIR_C
- U14 pad 14: /motor_driver5/DATA_OUT -> /motor_driver5/STEP_C
- U14 pad 15: /motor_driver6/DIR_A -> VCC
- U14 pad 16: VCC -> /motor_driver5/DIR_D
- U14 pad 2: /motor_driver6/STEP_D -> /motor_driver5/DIR_B
- U14 pad 3: /motor_driver6/STEP_A -> /motor_driver5/STEP_B
- U14 pad 4: /motor_driver6/STEP_C -> /motor_driver5/A3
- U14 pad 5: /motor_driver6/DIR_C -> /motor_driver5/A4
- U14 pad 6: /motor_driver6/STEP_B -> /motor_driver5/A2
- U14 pad 7: /motor_driver6/DIR_B -> /motor_driver5/A1
- U14 pad 8: GND -> /motor_driver5/D1
- U14 pad 9: /motor_driver6/DATA_OUT -> /motor_driver5/D2
- U15 pad 1: VCC -> /motor_driver6/STEP_D
- U15 pad 10: /motor_driver6/D4 -> VCC
- U15 pad 11: /motor_driver6/D3 -> SHIFT_CLOCK
- U15 pad 12: GND -> LATCH_CLOCK
- U15 pad 13: /motor_driver6/DIR_C -> GND
- U15 pad 14: /motor_driver6/STEP_C -> /motor_driver5/DATA_OUT
- U15 pad 15: VCC -> /motor_driver6/DIR_D
- U15 pad 16: /motor_driver6/DIR_D -> VCC
- U15 pad 2: /motor_driver6/DIR_B -> /motor_driver6/DIR_A
- U15 pad 3: /motor_driver6/STEP_B -> /motor_driver6/STEP_A
- U15 pad 4: /motor_driver6/A3 -> /motor_driver6/DIR_B
- U15 pad 5: /motor_driver6/A4 -> /motor_driver6/STEP_B
- U15 pad 6: /motor_driver6/A2 -> /motor_driver6/DIR_C
- U15 pad 7: /motor_driver6/A1 -> /motor_driver6/STEP_C
- U15 pad 8: /motor_driver6/D1 -> GND
- U15 pad 9: /motor_driver6/D2 -> /motor_driver6/DATA_OUT
- U16 pad 1: /motor_driver7/DIR_D -> VCC
- U16 pad 10: Reset -> /motor_driver6/D4
- U16 pad 11: SHIFT_CLOCK -> /motor_driver6/D3
- U16 pad 12: LATCH_CLOCK -> GND
- U16 pad 13: GND -> /motor_driver6/DIR_C
- U16 pad 14: /motor_driver6/DATA_OUT -> /motor_driver6/STEP_C
- U16 pad 15: /motor_driver7/DIR_A -> VCC
- U16 pad 16: VCC -> /motor_driver6/DIR_D
- U16 pad 2: /motor_driver7/STEP_D -> /motor_driver6/DIR_B
- U16 pad 3: /motor_driver7/STEP_A -> /motor_driver6/STEP_B
- U16 pad 4: /motor_driver7/STEP_C -> /motor_driver6/A3
- U16 pad 5: /motor_driver7/DIR_C -> /motor_driver6/A4
- U16 pad 6: /motor_driver7/STEP_B -> /motor_driver6/A2
- U16 pad 7: /motor_driver7/DIR_B -> /motor_driver6/A1
- U16 pad 8: GND -> /motor_driver6/D1
- U16 pad 9: /motor_driver7/DATA_OUT -> /motor_driver6/D2
- U17 pad 1: VCC -> /motor_driver7/STEP_D
- U17 pad 10: /motor_driver7/D4 -> VCC
- U17 pad 11: /motor_driver7/D3 -> SHIFT_CLOCK
- U17 pad 12: GND -> LATCH_CLOCK
- U17 pad 13: /motor_driver7/DIR_C -> GND
- U17 pad 14: /motor_driver7/STEP_C -> /motor_driver6/DATA_OUT
- U17 pad 15: VCC -> /motor_driver7/DIR_D
- U17 pad 16: /motor_driver7/DIR_D -> VCC
- U17 pad 2: /motor_driver7/DIR_B -> /motor_driver7/DIR_A
- U17 pad 3: /motor_driver7/STEP_B -> /motor_driver7/STEP_A
- U17 pad 4: /motor_driver7/A3 -> /motor_driver7/DIR_B
- U17 pad 5: /motor_driver7/A4 -> /motor_driver7/STEP_B
- U17 pad 6: /motor_driver7/A2 -> /motor_driver7/DIR_C
- U17 pad 7: /motor_driver7/A1 -> /motor_driver7/STEP_C
- U17 pad 8: /motor_driver7/D1 -> GND
- U17 pad 9: /motor_driver7/D2 -> /motor_driver7/DATA_OUT
- U18 pad 1: /motor_driver8/DIR_D -> VCC
- U18 pad 10: Reset -> /motor_driver7/D4
- U18 pad 11: SHIFT_CLOCK -> /motor_driver7/D3
- U18 pad 12: LATCH_CLOCK -> GND
- U18 pad 13: GND -> /motor_driver7/DIR_C
- U18 pad 14: /motor_driver7/DATA_OUT -> /motor_driver7/STEP_C
- U18 pad 15: /motor_driver8/DIR_A -> VCC
- U18 pad 16: VCC -> /motor_driver7/DIR_D
- U18 pad 2: /motor_driver8/STEP_D -> /motor_driver7/DIR_B
- U18 pad 3: /motor_driver8/STEP_A -> /motor_driver7/STEP_B
- U18 pad 4: /motor_driver8/STEP_C -> /motor_driver7/A3
- U18 pad 5: /motor_driver8/DIR_C -> /motor_driver7/A4
- U18 pad 6: /motor_driver8/STEP_B -> /motor_driver7/A2
- U18 pad 7: /motor_driver8/DIR_B -> /motor_driver7/A1
- U18 pad 8: GND -> /motor_driver7/D1
- U18 pad 9: /motor_driver8/DATA_OUT -> /motor_driver7/D2
- U19 pad 1: VCC -> /motor_driver8/STEP_D
- U19 pad 10: /motor_driver8/D4 -> VCC
- U19 pad 11: /motor_driver8/D3 -> SHIFT_CLOCK
- U19 pad 12: GND -> LATCH_CLOCK
- U19 pad 13: /motor_driver8/DIR_C -> GND
- U19 pad 14: /motor_driver8/STEP_C -> /motor_driver7/DATA_OUT
- U19 pad 15: VCC -> /motor_driver8/DIR_D
- U19 pad 16: /motor_driver8/DIR_D -> VCC
- U19 pad 2: /motor_driver8/DIR_B -> /motor_driver8/DIR_A
- U19 pad 3: /motor_driver8/STEP_B -> /motor_driver8/STEP_A
- U19 pad 4: /motor_driver8/A3 -> /motor_driver8/DIR_B
- U19 pad 5: /motor_driver8/A4 -> /motor_driver8/STEP_B
- U19 pad 6: /motor_driver8/A2 -> /motor_driver8/DIR_C
- U19 pad 7: /motor_driver8/A1 -> /motor_driver8/STEP_C
- U19 pad 8: /motor_driver8/D1 -> GND
- U19 pad 9: /motor_driver8/D2 -> /motor_driver8/DATA_OUT
- U2 pad 1: /motor_driver0/DIR_D -> LATCH_CLOCK
- U2 pad 2: /motor_driver0/STEP_D -> GND
- U2 pad 3: /motor_driver0/STEP_A -> /control_board/VCC_3V3
- U2 pad 4: /motor_driver0/STEP_C -> /control_board/LATCH_CLOCK_3V3
- U2 pad 5: /motor_driver0/DIR_C -> /control_board/SHIFT_CLOCK_3V3
- U2 pad 6: /motor_driver0/STEP_B -> GND
- U2 pad 7: /motor_driver0/DIR_B -> VCC
- U2 pad 8: GND -> SHIFT_CLOCK
- U20 pad 1: /motor_driver9/DIR_D -> VCC
- U20 pad 10: Reset -> /motor_driver8/D4
- U20 pad 11: SHIFT_CLOCK -> /motor_driver8/D3
- U20 pad 12: LATCH_CLOCK -> GND
- U20 pad 13: GND -> /motor_driver8/DIR_C
- U20 pad 14: /motor_driver8/DATA_OUT -> /motor_driver8/STEP_C
- U20 pad 15: /motor_driver9/DIR_A -> VCC
- U20 pad 16: VCC -> /motor_driver8/DIR_D
- U20 pad 2: /motor_driver9/STEP_D -> /motor_driver8/DIR_B
- U20 pad 3: /motor_driver9/STEP_A -> /motor_driver8/STEP_B
- U20 pad 4: /motor_driver9/STEP_C -> /motor_driver8/A3
- U20 pad 5: /motor_driver9/DIR_C -> /motor_driver8/A4
- U20 pad 6: /motor_driver9/STEP_B -> /motor_driver8/A2
- U20 pad 7: /motor_driver9/DIR_B -> /motor_driver8/A1
- U20 pad 8: GND -> /motor_driver8/D1
- U20 pad 9: /motor_driver10/DATA_IN -> /motor_driver8/D2
- U21 pad 1: VCC -> /motor_driver9/STEP_D
- U21 pad 10: /motor_driver9/D4 -> VCC
- U21 pad 11: /motor_driver9/D3 -> SHIFT_CLOCK
- U21 pad 12: GND -> LATCH_CLOCK
- U21 pad 13: /motor_driver9/DIR_C -> GND
- U21 pad 14: /motor_driver9/STEP_C -> /motor_driver8/DATA_OUT
- U21 pad 15: VCC -> /motor_driver9/DIR_D
- U21 pad 16: /motor_driver9/DIR_D -> VCC
- U21 pad 2: /motor_driver9/DIR_B -> /motor_driver9/DIR_A
- U21 pad 3: /motor_driver9/STEP_B -> /motor_driver9/STEP_A
- U21 pad 4: /motor_driver9/A3 -> /motor_driver9/DIR_B
- U21 pad 5: /motor_driver9/A4 -> /motor_driver9/STEP_B
- U21 pad 6: /motor_driver9/A2 -> /motor_driver9/DIR_C
- U21 pad 7: /motor_driver9/A1 -> /motor_driver9/STEP_C
- U21 pad 8: /motor_driver9/D1 -> GND
- U21 pad 9: /motor_driver9/D2 -> /motor_driver10/DATA_IN
- U22 pad 1: /motor_driver10/DIR_D -> VCC
- U22 pad 10: Reset -> /motor_driver9/D4
- U22 pad 11: SHIFT_CLOCK -> /motor_driver9/D3
- U22 pad 12: LATCH_CLOCK -> GND
- U22 pad 13: GND -> /motor_driver9/DIR_C
- U22 pad 14: /motor_driver10/DATA_IN -> /motor_driver9/STEP_C
- U22 pad 15: /motor_driver10/DIR_A -> VCC
- U22 pad 16: VCC -> /motor_driver9/DIR_D
- U22 pad 2: /motor_driver10/STEP_D -> /motor_driver9/DIR_B
- U22 pad 3: /motor_driver10/STEP_A -> /motor_driver9/STEP_B
- U22 pad 4: /motor_driver10/STEP_C -> /motor_driver9/A3
- U22 pad 5: /motor_driver10/DIR_C -> /motor_driver9/A4
- U22 pad 6: /motor_driver10/STEP_B -> /motor_driver9/A2
- U22 pad 7: /motor_driver10/DIR_B -> /motor_driver9/A1
- U22 pad 8: GND -> /motor_driver9/D1
- U22 pad 9: /motor_driver10/DATA_OUT -> /motor_driver9/D2
- U23 pad 1: VCC -> /motor_driver10/STEP_D
- U23 pad 10: /motor_driver10/D4 -> VCC
- U23 pad 11: /motor_driver10/D3 -> SHIFT_CLOCK
- U23 pad 12: GND -> LATCH_CLOCK
- U23 pad 13: /motor_driver10/DIR_C -> GND
- U23 pad 14: /motor_driver10/STEP_C -> /motor_driver10/DATA_IN
- U23 pad 15: VCC -> /motor_driver10/DIR_D
- U23 pad 16: /motor_driver10/DIR_D -> VCC
- U23 pad 2: /motor_driver10/DIR_B -> /motor_driver10/DIR_A
- U23 pad 3: /motor_driver10/STEP_B -> /motor_driver10/STEP_A
- U23 pad 4: /motor_driver10/A3 -> /motor_driver10/DIR_B
- U23 pad 5: /motor_driver10/A4 -> /motor_driver10/STEP_B
- U23 pad 6: /motor_driver10/A2 -> /motor_driver10/DIR_C
- U23 pad 7: /motor_driver10/A1 -> /motor_driver10/STEP_C
- U23 pad 8: /motor_driver10/D1 -> GND
- U23 pad 9: /motor_driver10/D2 -> /motor_driver10/DATA_OUT
- U24 pad 1: /motor_driver11/DIR_D -> VCC
- U24 pad 10: Reset -> /motor_driver10/D4
- U24 pad 11: SHIFT_CLOCK -> /motor_driver10/D3
- U24 pad 12: LATCH_CLOCK -> GND
- U24 pad 13: GND -> /motor_driver10/DIR_C
- U24 pad 14: /motor_driver10/DATA_OUT -> /motor_driver10/STEP_C
- U24 pad 15: /motor_driver11/DIR_A -> VCC
- U24 pad 16: VCC -> /motor_driver10/DIR_D
- U24 pad 2: /motor_driver11/STEP_D -> /motor_driver10/DIR_B
- U24 pad 3: /motor_driver11/STEP_A -> /motor_driver10/STEP_B
- U24 pad 4: /motor_driver11/STEP_C -> /motor_driver10/A3
- U24 pad 5: /motor_driver11/DIR_C -> /motor_driver10/A4
- U24 pad 6: /motor_driver11/STEP_B -> /motor_driver10/A2
- U24 pad 7: /motor_driver11/DIR_B -> /motor_driver10/A1
- U24 pad 8: GND -> /motor_driver10/D1
- U24 pad 9: /motor_driver11/DATA_OUT -> /motor_driver10/D2
- U25 pad 1: VCC -> /motor_driver11/STEP_D
- U25 pad 10: /motor_driver11/D4 -> VCC
- U25 pad 11: /motor_driver11/D3 -> SHIFT_CLOCK
- U25 pad 12: GND -> LATCH_CLOCK
- U25 pad 13: /motor_driver11/DIR_C -> GND
- U25 pad 14: /motor_driver11/STEP_C -> /motor_driver10/DATA_OUT
- U25 pad 15: VCC -> /motor_driver11/DIR_D
- U25 pad 16: /motor_driver11/DIR_D -> VCC
- U25 pad 2: /motor_driver11/DIR_B -> /motor_driver11/DIR_A
- U25 pad 3: /motor_driver11/STEP_B -> /motor_driver11/STEP_A
- U25 pad 4: /motor_driver11/A3 -> /motor_driver11/DIR_B
- U25 pad 5: /motor_driver11/A4 -> /motor_driver11/STEP_B
- U25 pad 6: /motor_driver11/A2 -> /motor_driver11/DIR_C
- U25 pad 7: /motor_driver11/A1 -> /motor_driver11/STEP_C
- U25 pad 8: /motor_driver11/D1 -> GND
- U25 pad 9: /motor_driver11/D2 -> /motor_driver11/DATA_OUT
- U3 pad 1: VCC -> /motor_driver0/STEP_D
- U3 pad 10: /motor_driver0/D4 -> VCC
- U3 pad 11: /motor_driver0/D3 -> SHIFT_CLOCK
- U3 pad 12: GND -> LATCH_CLOCK
- U3 pad 13: /motor_driver0/DIR_C -> GND
- U3 pad 14: /motor_driver0/STEP_C -> /control_board/DATA_OUT
- U3 pad 15: VCC -> /motor_driver0/DIR_D
- U3 pad 16: /motor_driver0/DIR_D -> VCC
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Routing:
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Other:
- board outline added: 226.2 x 90.5 mm
